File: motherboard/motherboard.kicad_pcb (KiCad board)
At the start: 2 copper layers, 40 parts, among them J1 Raspberry_Pi_2_3 ANT, J2 PROGRAM, J3 Battery / Pitot/ Orientation, J4 c02 censor, J5 shaftencorder, J6 USB_C_Receptacle_USB2.0, J7 SparLoad, J8 lidar, J9 Control Board, Q1 2N7002K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

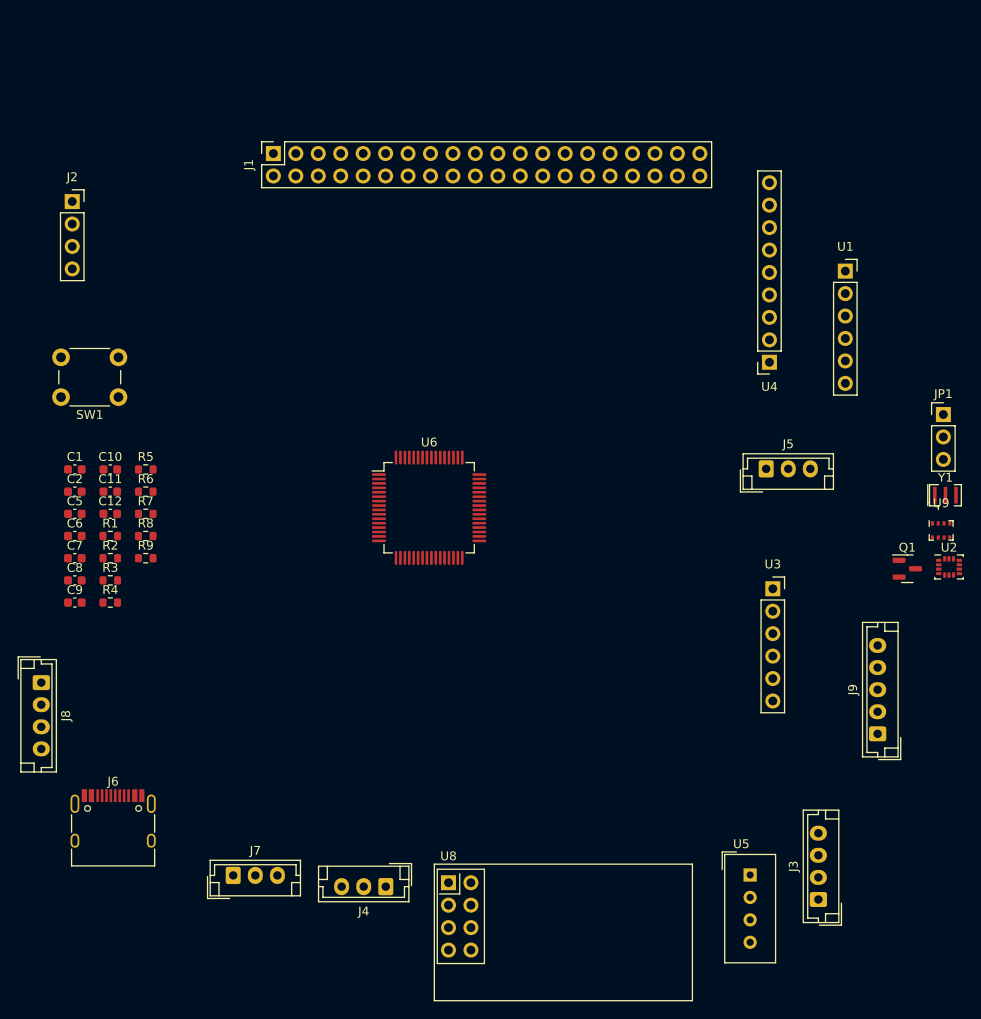
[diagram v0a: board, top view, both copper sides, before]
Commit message: Edited footprints
Edited custom footprints and completed first layout draft
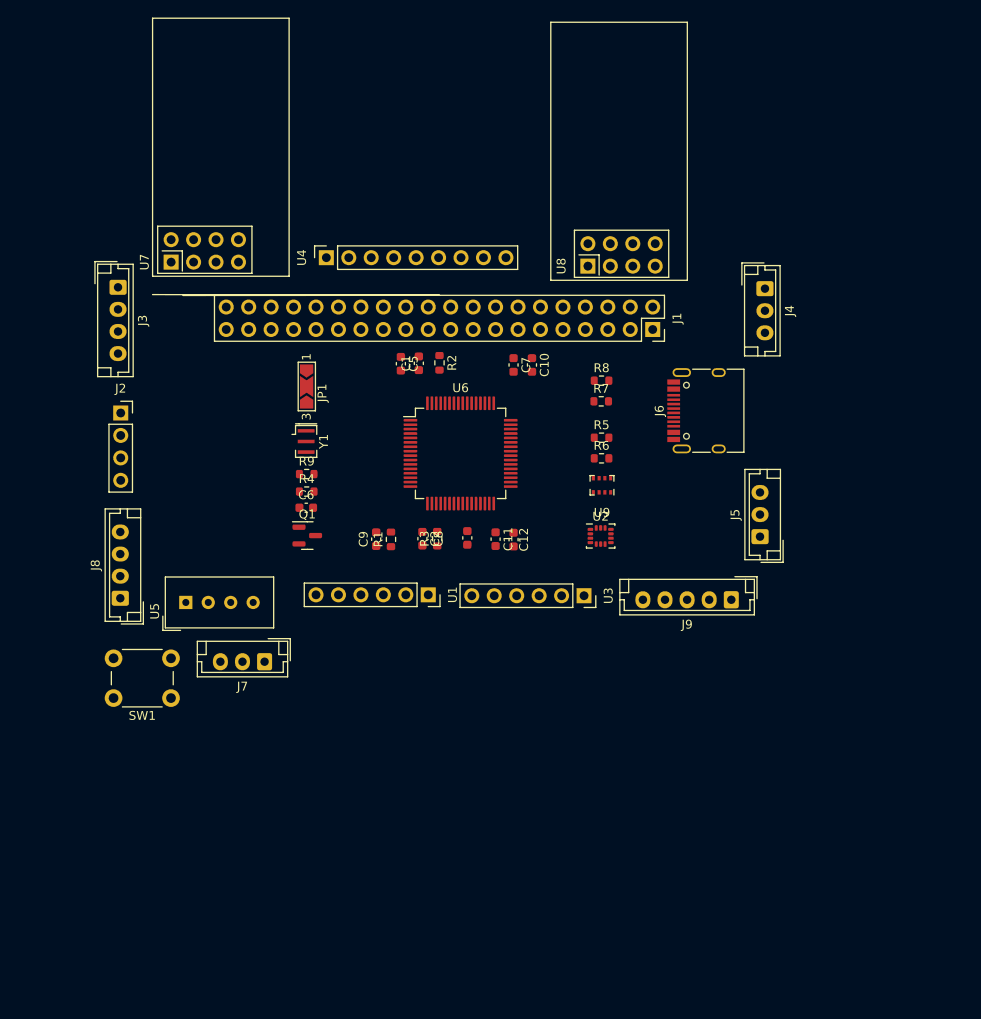
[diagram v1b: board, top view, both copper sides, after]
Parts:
- added U7: nRF24L01-telemetry-INTERIOR, RF_Module:nRF24L01_Breakout, F.Cu at (81.5, 66.0)
- JP1: footprint Connector_PinHeader_2.54mm:PinHeader_1x03_P2.54mm_Vertical -> Jumper:SolderJumper-3_P2.0mm_Open_TrianglePad1.0x1.5mm_NumberLabels
- U8: value nRF24L01-telemetry -> nRF24L01-telemetry-EXTERIOR
- moved J3 105.3 mm to (75.5, 68.9), turned to -90 degrees
- moved J6 82.6 mm to (142.5, 82.9), turned to 90 degrees
- moved J4 80.1 mm to (148.7, 69.0), turned to -90 degrees
- moved Y1 72.6 mm to (96.8, 86.3), turned to -90 degrees
- moved JP1 72.1 mm to (96.9, 80.1), turned to -90 degrees
- moved U8 71.5 mm to (128.7, 66.5), turned to 90 degrees
- moved U5 70.9 mm to (83.2, 104.5), turned to 90 degrees
- moved Q1 68.0 mm to (97.0, 97.0)
- moved U1 59.7 mm to (110.6, 103.7), turned to -90 degrees
- moved R8 54.5 mm to (130.3, 79.5)
- moved C7 54.2 mm to (120.3, 77.7), turned to -90 degrees
- moved R7 53.1 mm to (130.2, 81.8)
- moved R6 51.7 mm to (130.3, 88.2)
- moved R5 51.7 mm to (130.3, 85.9)
- moved U4 51.5 mm to (99.1, 65.5), turned to 90 degrees
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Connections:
- net /TELE_{CE} renamed /TELE_{CE}-E
- net /TELE_{CS} renamed /TELE_{CS}-E
- net /TELE_{IRQ} renamed /TELE_{IRQ}-E
- U6 pad 56: unconnected-(U6-PB4-Pad56) -> /TELE_{IRQ}-int
- U6 pad 57: unconnected-(U6-PB5-Pad57) -> /TELE_{CE}-int
- U6 pad 62: unconnected-(U6-PB9-Pad62) -> /TELE_{CS}-int

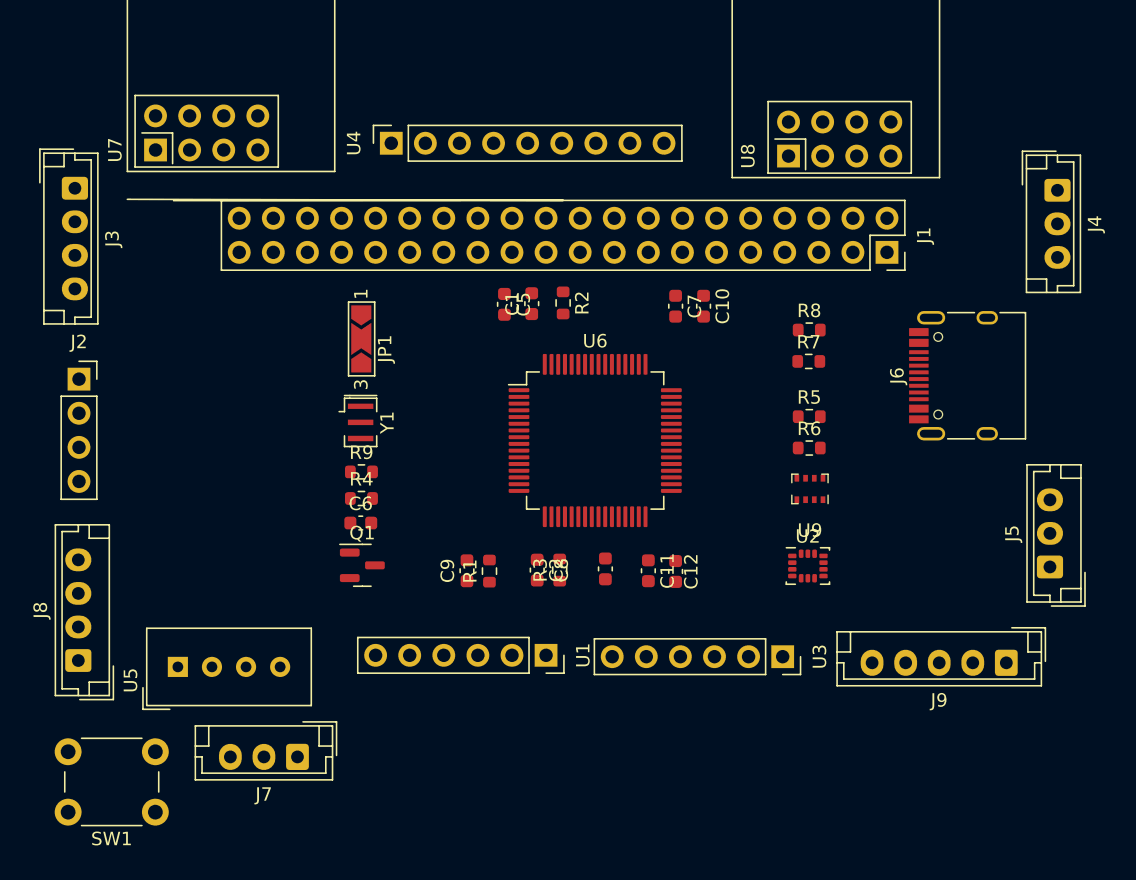
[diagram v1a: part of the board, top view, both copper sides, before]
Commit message: Added Traces
Added more traces to the layout
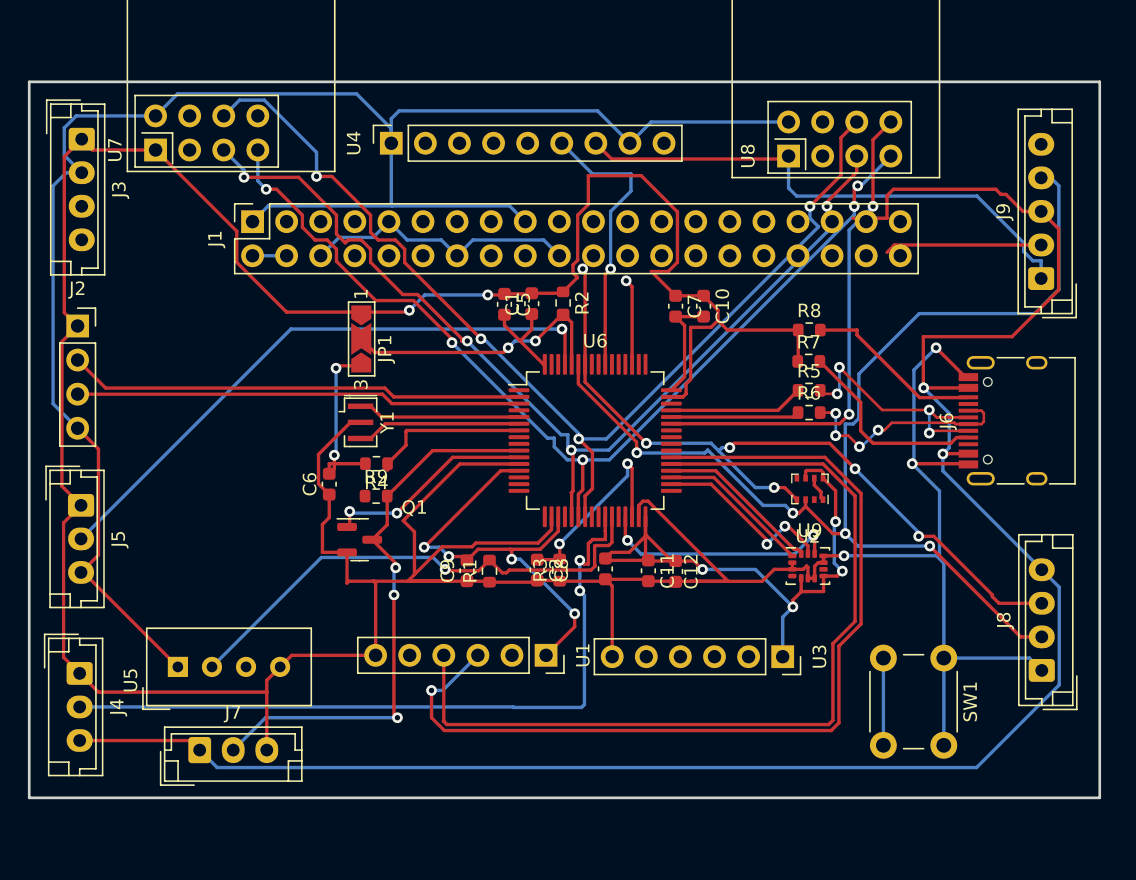
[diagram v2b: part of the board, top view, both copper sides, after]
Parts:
- moved J4 81.3 mm to (75.9, 105.0)
- moved J5 72.3 mm to (76.0, 92.5), turned to -90 degrees
- moved J8 71.8 mm to (147.6, 104.8)
- moved SW1 59.9 mm to (140.3, 103.9), turned to -90 degrees
- moved J1 47.3 mm to (88.8, 71.4), turned to 90 degrees
- moved J9 28.7 mm to (147.5, 75.6), turned to 90 degrees
- moved J7 7.30 mm to (84.8, 110.7), turned to 0 degrees
- moved J6 4.99 mm to (146.2, 86.2)
- moved J2 3.96 mm to (75.7, 79.1)
- moved C6 3.73 mm to (94.5, 90.9), turned to 90 degrees
- moved J3 3.69 mm to (76.0, 65.2)
- moved R4 2.82 mm to (98.0, 89.4), turned to 180 degrees
- moved R6 2.64 mm to (130.2, 85.6)
- moved R9 2.11 mm to (98.0, 91.8)
- moved R5 1.96 mm to (130.2, 83.9)
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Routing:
- net GND: track 0.00 -> 391.5 mm, vias 0 -> 5
- net +3.3V: track 0.00 -> 255.6 mm, vias 0 -> 10
- net +5V: track 0.00 -> 149.2 mm, vias 0 -> 2
- net /I2C_{SDA}: track 0.00 -> 84.8 mm, vias 0 -> 4
- net /SPI1MOSI: track 0.00 -> 80.4 mm, vias 0 -> 4
- net /SPI1SCK: track 0.00 -> 75.1 mm, vias 0 -> 4
- net /SPI1MISO: track 0.00 -> 74.5 mm, vias 0 -> 5
- net /USART6_{RX}: track 0.00 -> 70.6 mm, vias 0 -> 1
- net /USART6_{TX}: track 0.00 -> 66.2 mm
- net /I2C_{SCK}: track 0.00 -> 57.4 mm, vias 0 -> 6
- net /CO_{2}: track 0.00 -> 54.0 mm, vias 0 -> 2
- net /SHAFTENC: track 0.00 -> 45.0 mm, vias 0 -> 1
- net /OneWire_{RX}: track 0.00 -> 42.3 mm, vias 0 -> 3
- net /DHT22: track 0.00 -> 38.1 mm, vias 0 -> 1
- net /TELE_{IRQ}-E: track 0.00 -> 36.6 mm, vias 0 -> 2
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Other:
- board outline added: 79.8 x 53.3 mm

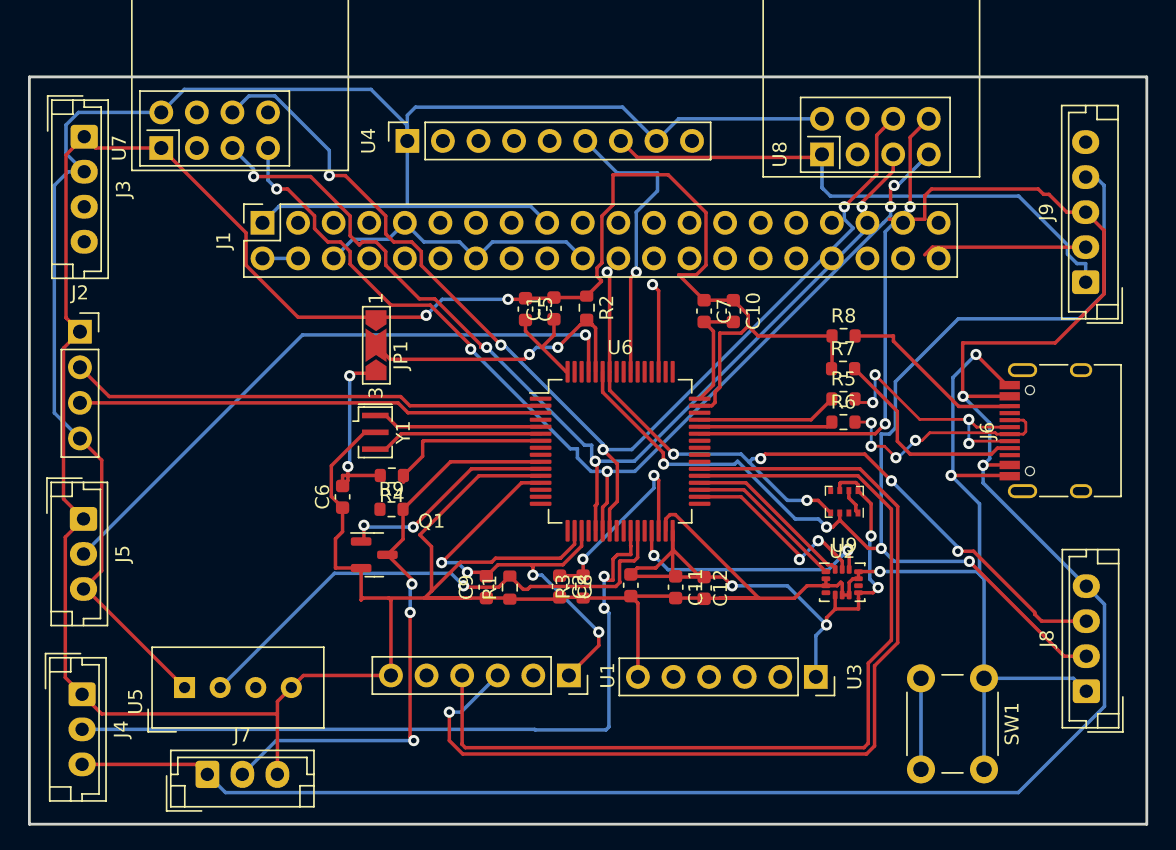
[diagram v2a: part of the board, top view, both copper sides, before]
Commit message: Completed draft 1 of layout
Finished laying down traces and running drc on the layout
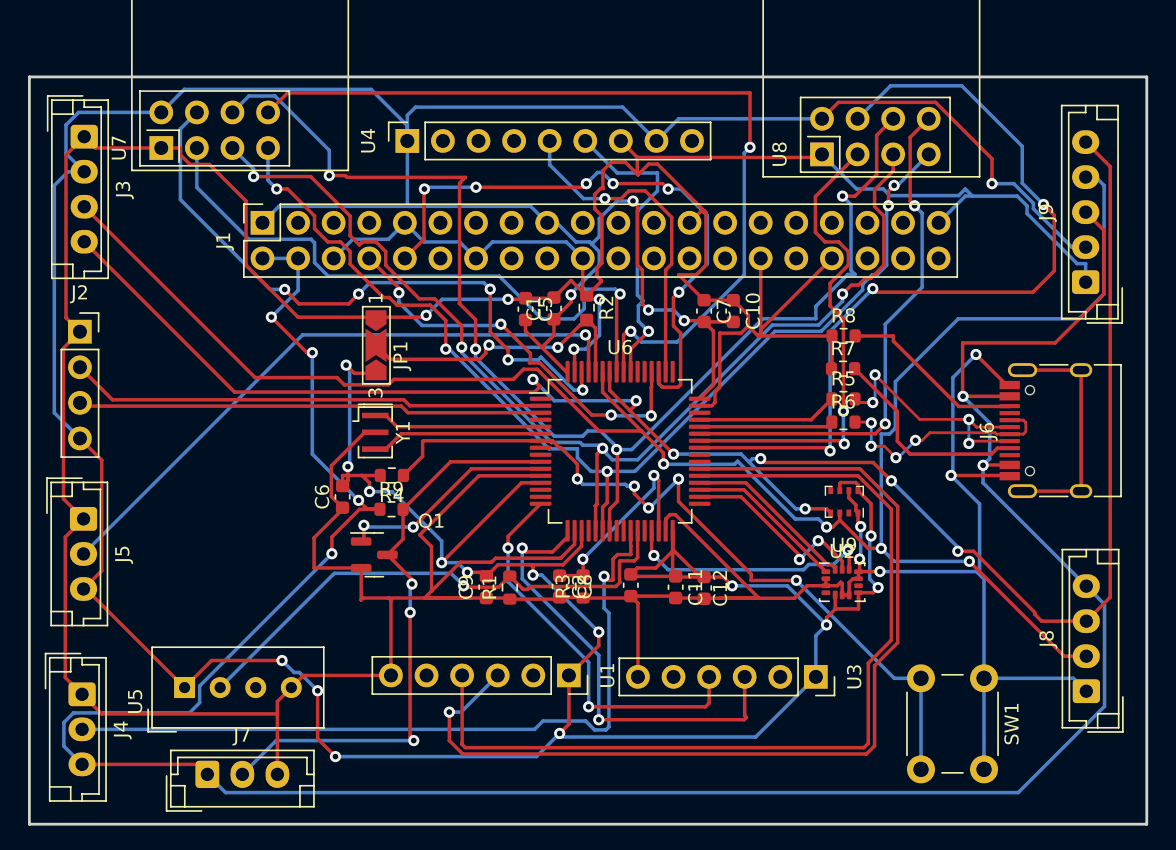
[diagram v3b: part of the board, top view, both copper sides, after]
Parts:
- J1: value Raspberry_Pi_2_3 ANT -> locked
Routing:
- net +3.3V: track 255.6 -> 365.9 mm, vias 10 -> 20
- net /I2C_{SCK}: track 57.4 -> 132.3 mm, vias 6 -> 7
- net /TELE_{IRQ}-int: track 0.00 -> 61.8 mm, vias 0 -> 2
- net /TELE_{CS}-E: track 0.00 -> 60.3 mm, vias 0 -> 3
- net /I2C_{SDA}: track 84.8 -> 132.1 mm
- net /TELE_{CS}-int: track 0.00 -> 46.0 mm, vias 0 -> 5
- net /TELE_{CE}-int: track 0.00 -> 45.2 mm, vias 0 -> 1
- net +5V: track 149.2 -> 189.0 mm, vias 2 -> 6
- net GND: track 391.5 -> 431.2 mm, vias 5 -> 9
- net /RST: track 18.0 -> 56.0 mm, vias 0 -> 5
- net /USART3_{TX}: track 6.59 -> 43.4 mm, vias 1 -> 6
- net /TELE_{CE}-E: track 0.00 -> 34.8 mm, vias 0 -> 2
- net /USART2_{RX}: track 0.00 -> 32.3 mm, vias 0 -> 2
- net /USART3_{RX}: track 0.00 -> 29.1 mm, vias 0 -> 4
- net /USART2_{TX}: track 0.00 -> 28.4 mm, vias 0 -> 2
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
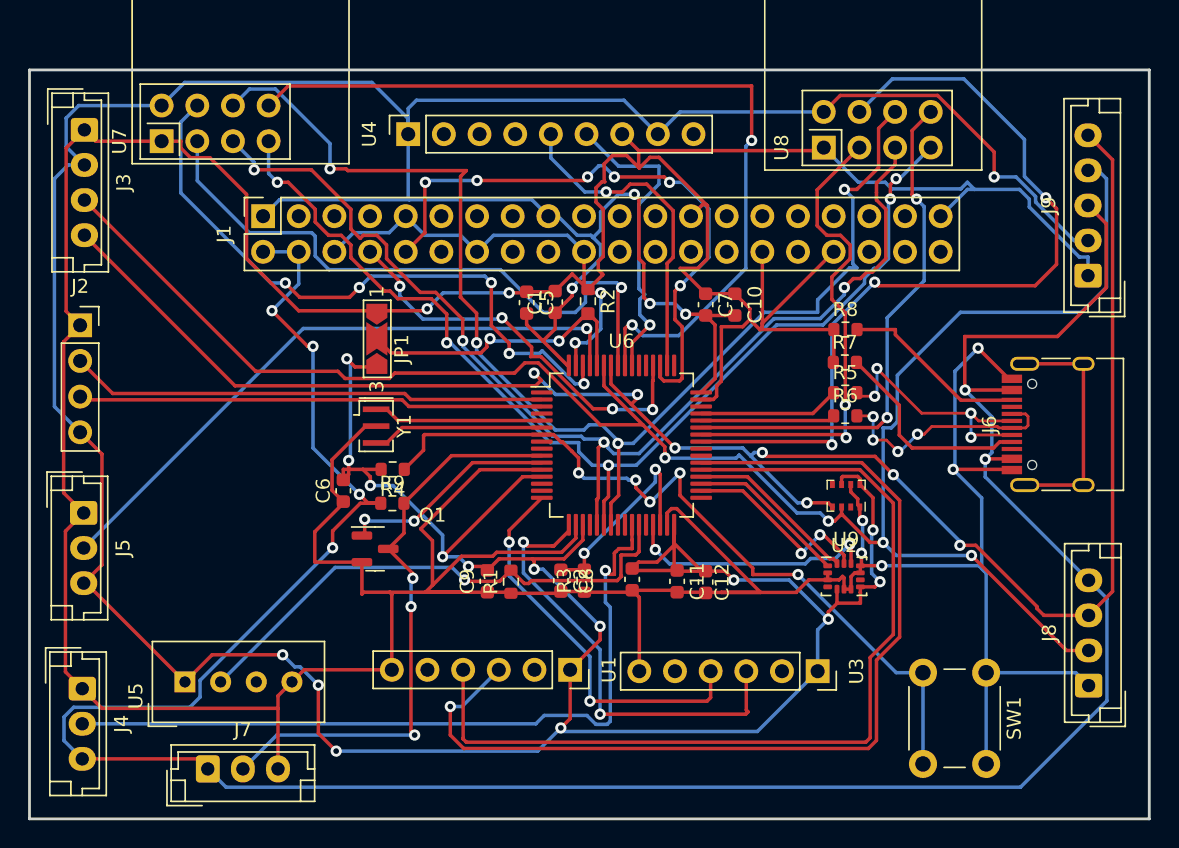
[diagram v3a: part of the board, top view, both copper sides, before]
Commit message: Polished 1st Draft Layout
Aligned vias, grouped traces, added text and graphics
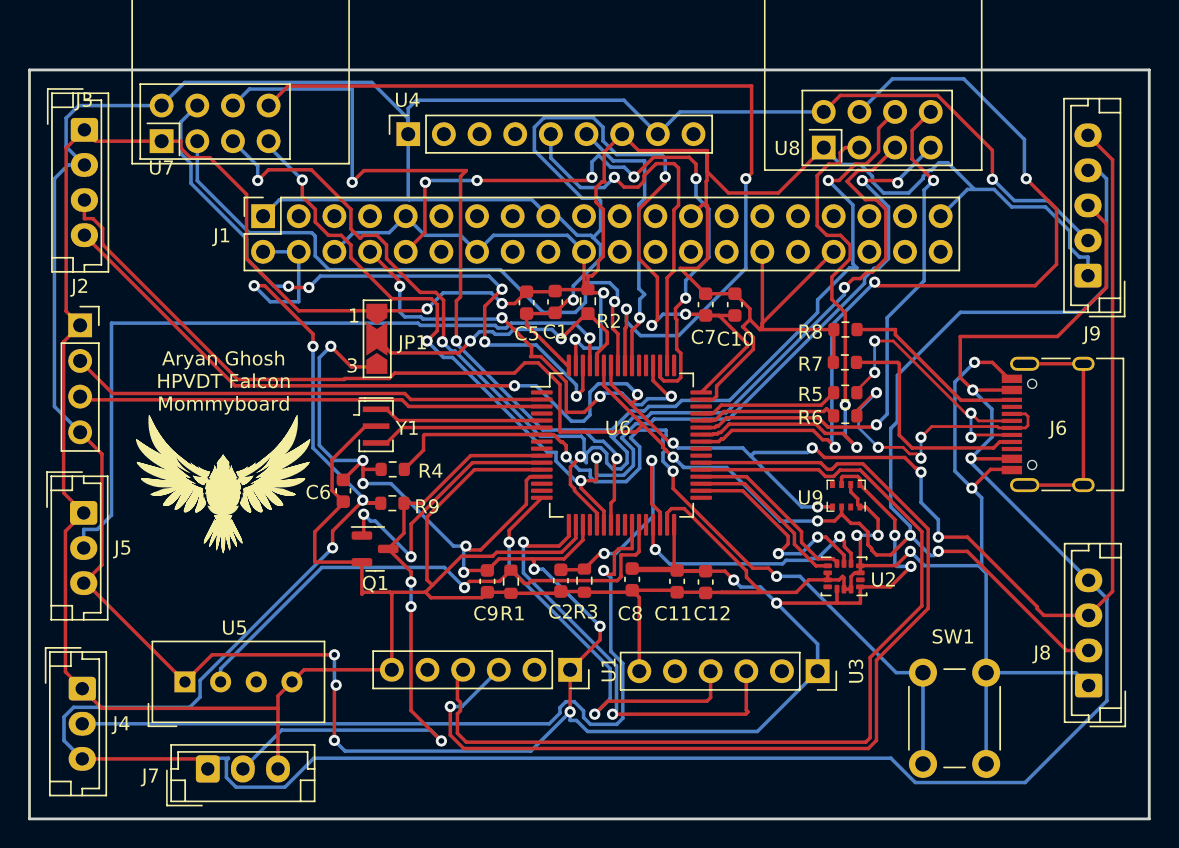
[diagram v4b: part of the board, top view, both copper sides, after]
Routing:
- net +3.3V: track 365.9 -> 395.9 mm
- net /SPI1SCK: track 79.8 -> 90.2 mm
- net +5V: track 189.0 -> 198.7 mm
- net /SPI1MISO: track 77.7 -> 87.0 mm, vias 5 -> 6
- net /SHAFTENC: track 45.0 -> 54.2 mm
- net /SPI1MOSI: track 89.5 -> 96.2 mm
- net /D+: track 17.0 -> 22.1 mm
- net /I2C_{SDA}: track 132.1 -> 137.0 mm
- net /RST: track 56.0 -> 60.6 mm, vias 5 -> 3
- net /USART3_{RX}: track 29.1 -> 33.3 mm
- net /USART1_{TX}: track 23.6 -> 27.7 mm
- net /OneWire_{TX}: track 15.6 -> 19.6 mm
- net /TELE_{CE}-E: track 34.8 -> 38.6 mm
- net /USART3_{TX}: track 43.4 -> 46.9 mm
- net /I2C_{SCK}: track 132.3 -> 135.8 mm
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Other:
- board text added: "Aryan Ghosh HPVDT Falcon Mommyboard"
